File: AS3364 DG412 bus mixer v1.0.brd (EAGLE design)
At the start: 81.3 x 36.7 mm, 148 parts, among them IC1 PCA9539PW, IC10 DG412-J, IC11 DG412-J, IC14 TL074JT, IC2 TL074JT, IC3 TL072JT, IC4 TL074JT, IC6 TL072JT, IC8 DG412-J, IC9 DG412-J

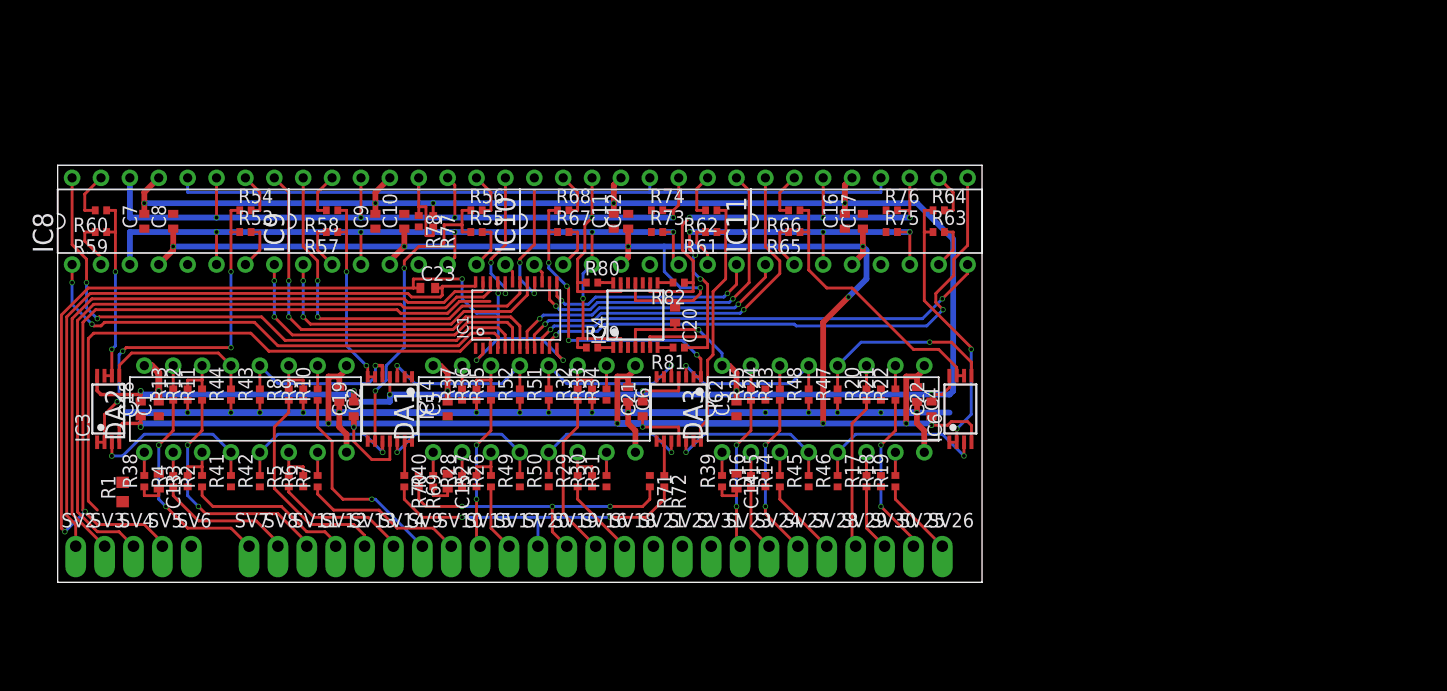
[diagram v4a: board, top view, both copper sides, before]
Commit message: Mostly traced, need to do ground and cleanup
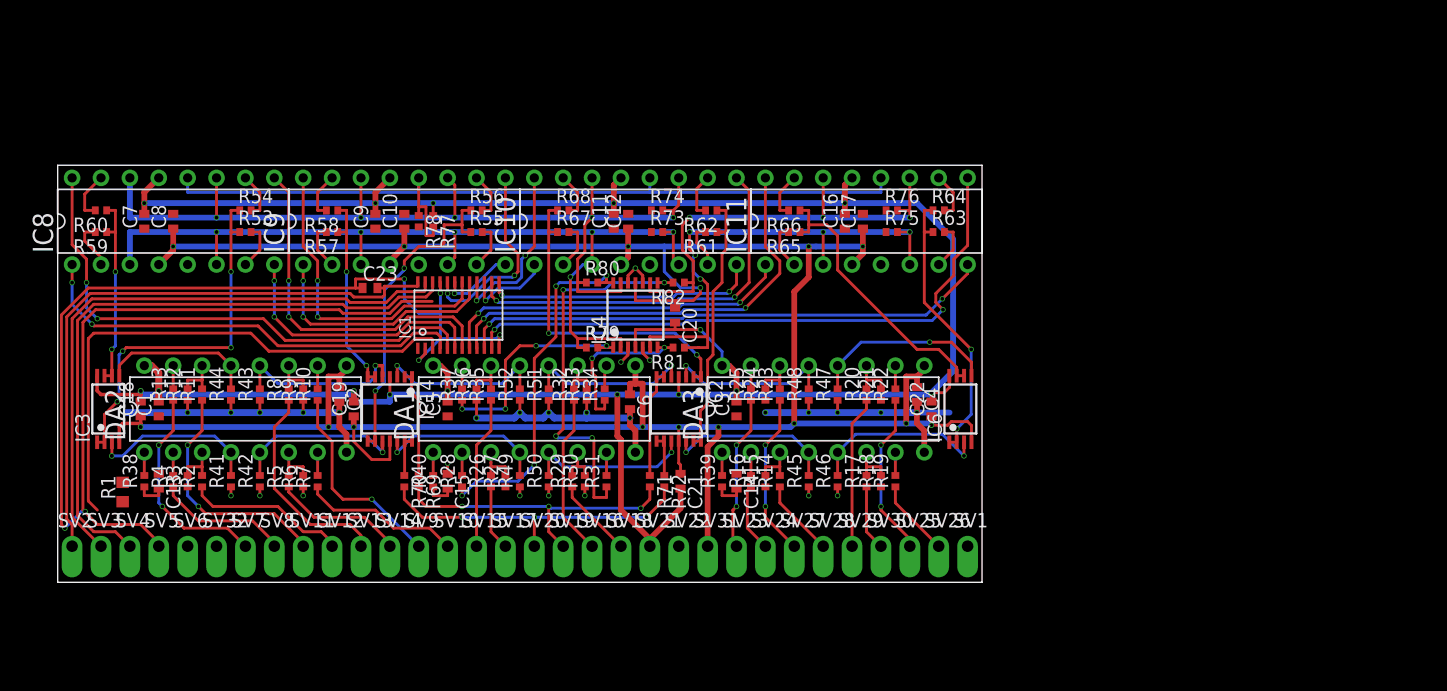
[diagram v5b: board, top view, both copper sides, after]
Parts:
- added SV1, SV32: (no value), joakim:SIP-PIN01-1J
- moved C21 7.17 mm to (54.8, 8.89), turned to 270 degrees
- moved C23 5.08 mm to (27.5, 25.9)
- moved IC1 5.08 mm to (35.2, 23.5)
- moved R27 2.54 mm to (39.4, 8.89)
- moved C6 0.65 mm to (50.3, 15.9)
- moved R30 0.64 mm to (46.4, 8.89)
- moved R29 0.48 mm to (45.2, 8.89)
- moved R33 0.48 mm to (46.5, 16.5)
- moved SV27 0.32 mm to (64.8, 3.17)
- moved SV29 0.32 mm to (69.8, 3.17)
- moved SV10 0.32 mm to (34.3, 3.17)
- moved SV12 0.32 mm to (24.1, 3.17)
- moved SV15 0.32 mm to (36.8, 3.17)
- moved SV17 0.32 mm to (39.4, 3.17)
- moved SV20 0.32 mm to (41.9, 3.17)
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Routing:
- net SUM_FX_B: track 1.37 -> 34.2 mm, vias 0 -> 4
- net SUM_B: track 1.37 -> 31.7 mm, vias 0 -> 4
- net GND: track 110.7 -> 87.6 mm, vias 15 -> 27
- net SUM_A: track 1.42 -> 19.9 mm, vias 0 -> 4
- net +12V: track 217.3 -> 232.4 mm, vias 14 -> 15
- net SUM_FX_A: track 1.37 -> 14.3 mm, vias 0 -> 2
- net DGND: track 143.4 -> 131.2 mm
- net -12V: track 242.8 -> 231.3 mm, vias 14 -> 15
- net OUT_A: track 0.65 -> 9.59 mm
- net OUT_FX_A: track 0.65 -> 9.57 mm
- net DIG_5_BUS_A: track 1.81 -> 7.76 mm, vias 0 -> 1
- net DIG_7_BUS_B: track 34.0 -> 39.5 mm
- net DIG_7_BUS_A: track 25.5 -> 31.1 mm
- net DIG_8_BUS_A: track 41.5 -> 47.0 mm
- net DIG_8_BUS_B: track 49.5 -> 54.9 mm
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
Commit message: Finished tracing, need part numbers
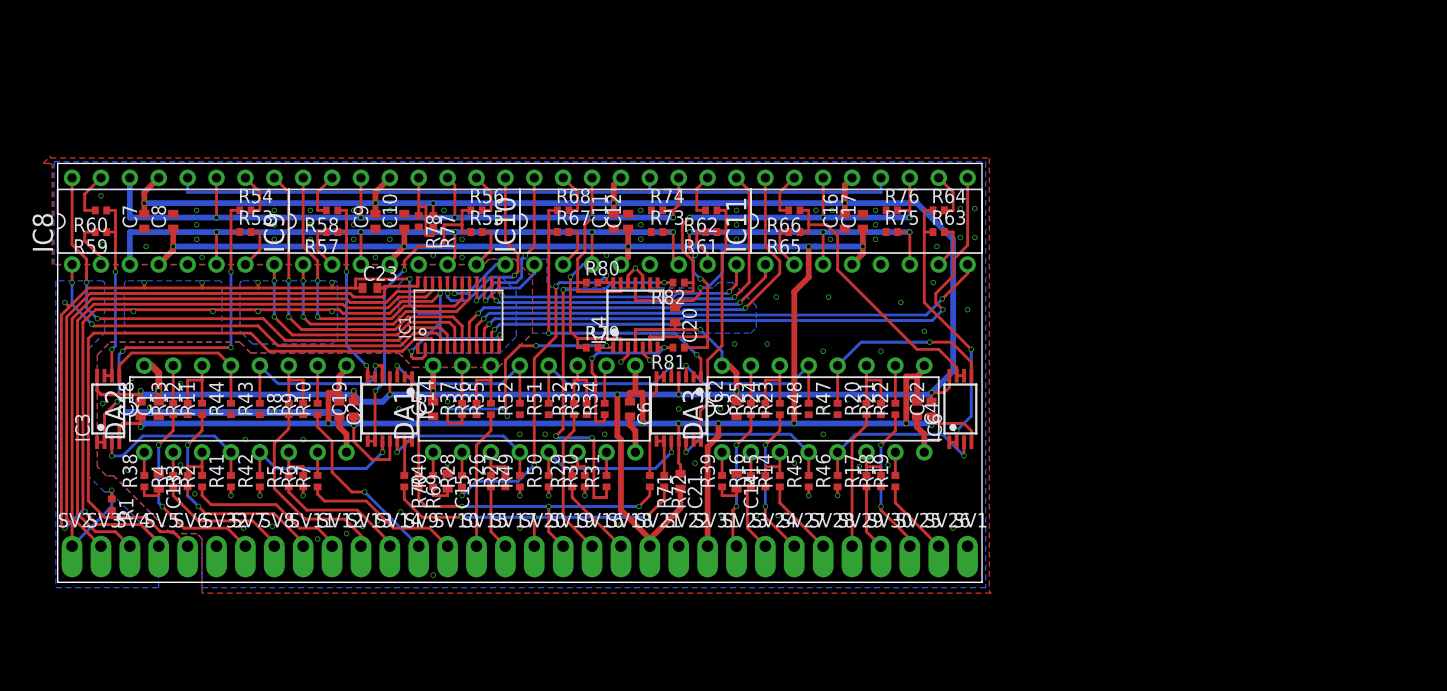
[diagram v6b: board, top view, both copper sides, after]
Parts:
- R1: value 1K -> 10k; device rcl:R0603 -> rcl:R0402
- moved R1 1.46 mm to (4.76, 6.83), turned to 270 degrees
- moved C2 1.27 mm to (24.8, 15.2)
- moved C4 1.27 mm to (75.6, 15.2)
- moved R10 1.27 mm to (22.9, 15.2)
- moved R11 1.27 mm to (12.7, 15.2)
- moved R12 1.27 mm to (11.4, 15.2)
- moved R13 1.27 mm to (10.2, 15.2)
- moved R20 1.27 mm to (71.1, 15.2)
- moved R21 1.27 mm to (72.4, 15.2)
- moved R22 1.27 mm to (73.7, 15.2)
- moved R23 1.27 mm to (63.5, 15.2)
- moved R24 1.27 mm to (62.2, 15.2)
- moved R25 1.27 mm to (61.0, 15.2)
- moved R32 1.27 mm to (45.4, 15.2)
- moved R33 1.27 mm to (46.5, 15.2)
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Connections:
- net N$4 renamed VL
- removed net N$81: IC1.3, R1.2
- removed net RST: SV6.1
- new net !RST: IC1.3, R1.2, SV6.1
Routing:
- net !RST: track 0.00 -> 57.6 mm
- net N$81: track 47.8 -> 0.00 mm
- net GND: track 87.6 -> 43.1 mm, vias 27 -> 104
- net +3V3: track 54.0 -> 61.2 mm, vias 0 -> 1
- net DGND: track 131.2 -> 137.8 mm, vias 6 -> 15
- net SUM_A: track 19.9 -> 23.5 mm
- net N$7: track 4.08 -> 6.62 mm
- net N$5: track 4.08 -> 6.62 mm
- net N$21: track 4.08 -> 6.62 mm
- net N$15: track 4.08 -> 6.62 mm
- net N$13: track 3.92 -> 6.46 mm
- net N$12: track 4.08 -> 6.62 mm
- net IN3: track 18.0 -> 15.9 mm
- net +12V: track 232.4 -> 230.8 mm
- net CV3: track 18.7 -> 17.3 mm
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- added copper zone on layer 16, net DGND
- added copper zone on layer 1, net GND
- added copper zone on layer 16, net GND
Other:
- board size 81.3 x 36.7 mm -> 81.3 x 36.8 mm

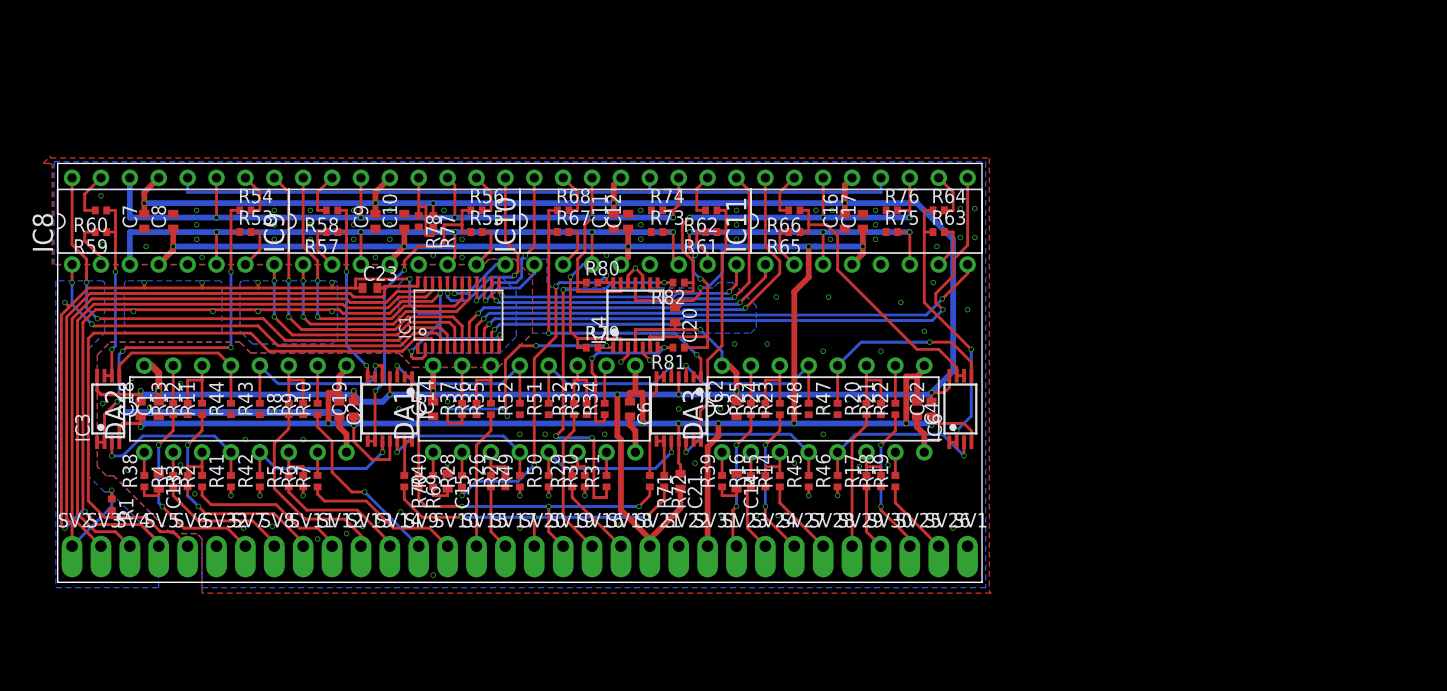
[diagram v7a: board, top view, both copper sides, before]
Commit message: All labels and names fixed
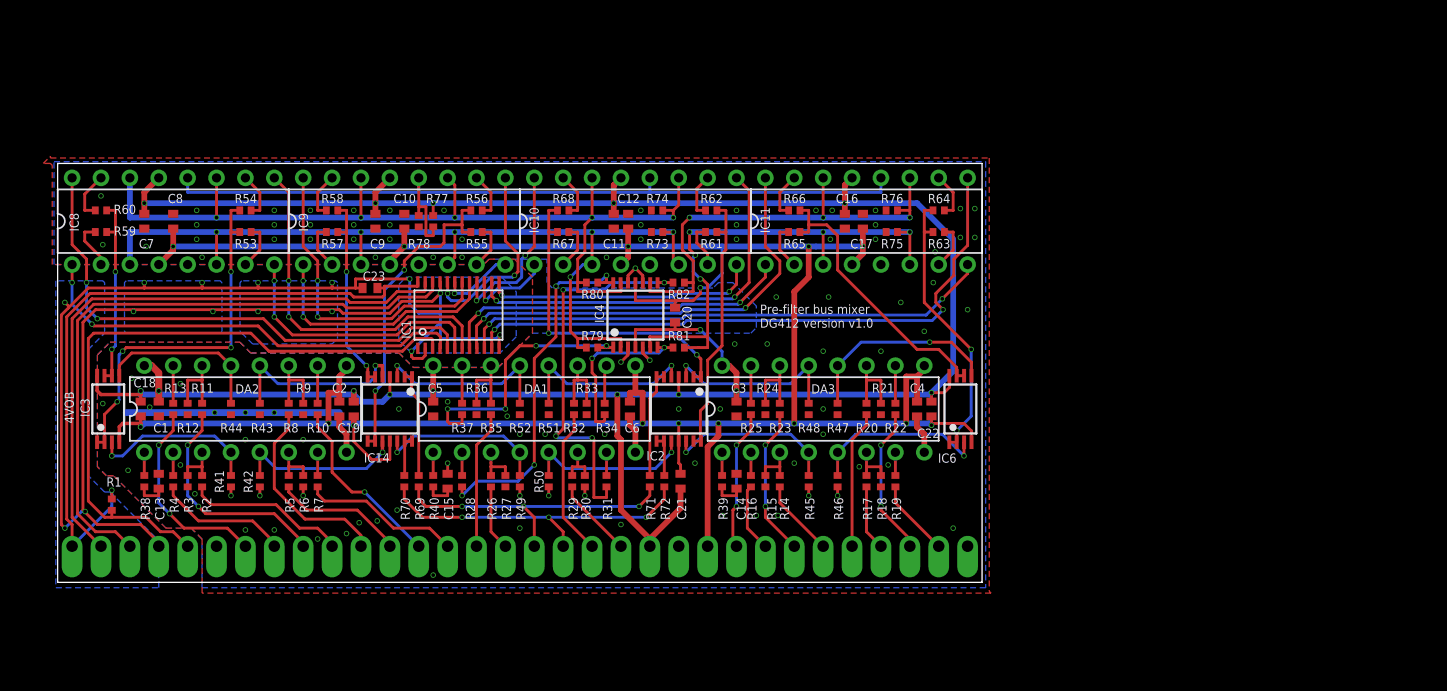
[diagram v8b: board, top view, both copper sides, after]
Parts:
- added U$1: (no value), joakim:XONIK_LOGO_35
- moved SV19 2.54 mm to (41.9, 3.17)
- moved SV20 2.54 mm to (44.5, 3.17)
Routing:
- net GND: track 43.1 -> 42.1 mm
- net LPF_IN_100K_MIX: track 28.9 -> 29.4 mm
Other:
- board text added: "+12V"
- board text added: "+3V3"
- board text added: "-12V"
- board text added: "4VOB"
- board text added: "AGND"
- board text added: "CV 1"
- board text added: "CV 2"
- board text added: "CV 3"
- board text added: "CV 4"
- board text added: "CV 5"
- board text added: "CV 6"
- board text added: "CV 7"
- board text added: "CV 8"
- board text added: "CV A"
- board text added: "CV B"
- board text added: "CV FX A"
- board text added: "CV FX B"
- board text added: "DGND"
- board text added: "In 1"
- board text added: "In 2"
- board text added: "In 3"
- board text added: "In 4"
- board text added: "In 5"
- board text added: "In 6"
- board text added: "In 7"
- board text added: "In 8"
- board text added: "OUT A"
- board text added: "OUT B"
- board text added: "Pre-filter bus mixer DG412 version v1.0"
- board text added: "RST"
- board text added: "SCL"
- board text added: "SDA"
